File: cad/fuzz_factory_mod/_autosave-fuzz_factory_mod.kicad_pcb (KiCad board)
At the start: 4 copper layers, 138 x 114 mm, 390 parts, among them J101 Conn_interface_1, J102 Conn_interface_2, J1701 Barrel_Jack_Switch, J1702 Conn_Battery, J1703 CONN_AUDIO_IN, J1704 CONN_AUDIO_OUT, J201 Conn_MCU_SWD, J2801 CONN_AUDIO_OUT_REF, J2802 CONN_EXP_1, J2803 CONN_EXP_2, J301 USB_B_Micro, J401 USB_B_Micro, J901 CONN_MIDI_IN, J902 CONN_MIDI_THRU, J903 CONN_MIDI_OUT, J904 Conn_01x10_Female, J905 Conn_01x10_Female, K2101 Fujitsu-Takamisawa-A_AL, Q1301 MMDT3904, Q1302 MMDT3904, Q1602 DTA123Y, Q1603 DTA123Y, Q1604 DTA123Y, Q1605 DTA123Y, Q1701 DTC114Y, Q1702 DTA114E, Q2201 BCP51, Q601 DTA123Y, Q602 DTA123Y, Q603 DTA123Y, Q604 DTA123Y, Q801 MMDT3904, Q802 MMDT3904, SW1101 SW_PUSH, SW1201 SW_PUSH, SW1301 SW_PUSH, U1101 LM1458, U1102 MC33202, U1201 LM2903, U1202 MC33202, U1501 LM1458, U1502 MC33202, U1503 MC33202, U1601 4050, U1602 4049, U1603 4504, U1604 MC33202, U1701 LM1458, U1702 MC33202, U1803 LM1458, U1804 MC33202, U1901 LM2903, U201 STM32F303VCTx, U2201 TL072, U2202 LM2674M-ADJ, U2203 LM78L05_SO8, U301 USBLC6-2SC6, U302 FT230XS, U401 USBLC6-2SC6, U501 74LS132, U601 4050, U602 4504, U603 MC33202, U604 4049, U701 AD5262_ABC, U901 4N25, Y201 Resonator_Small

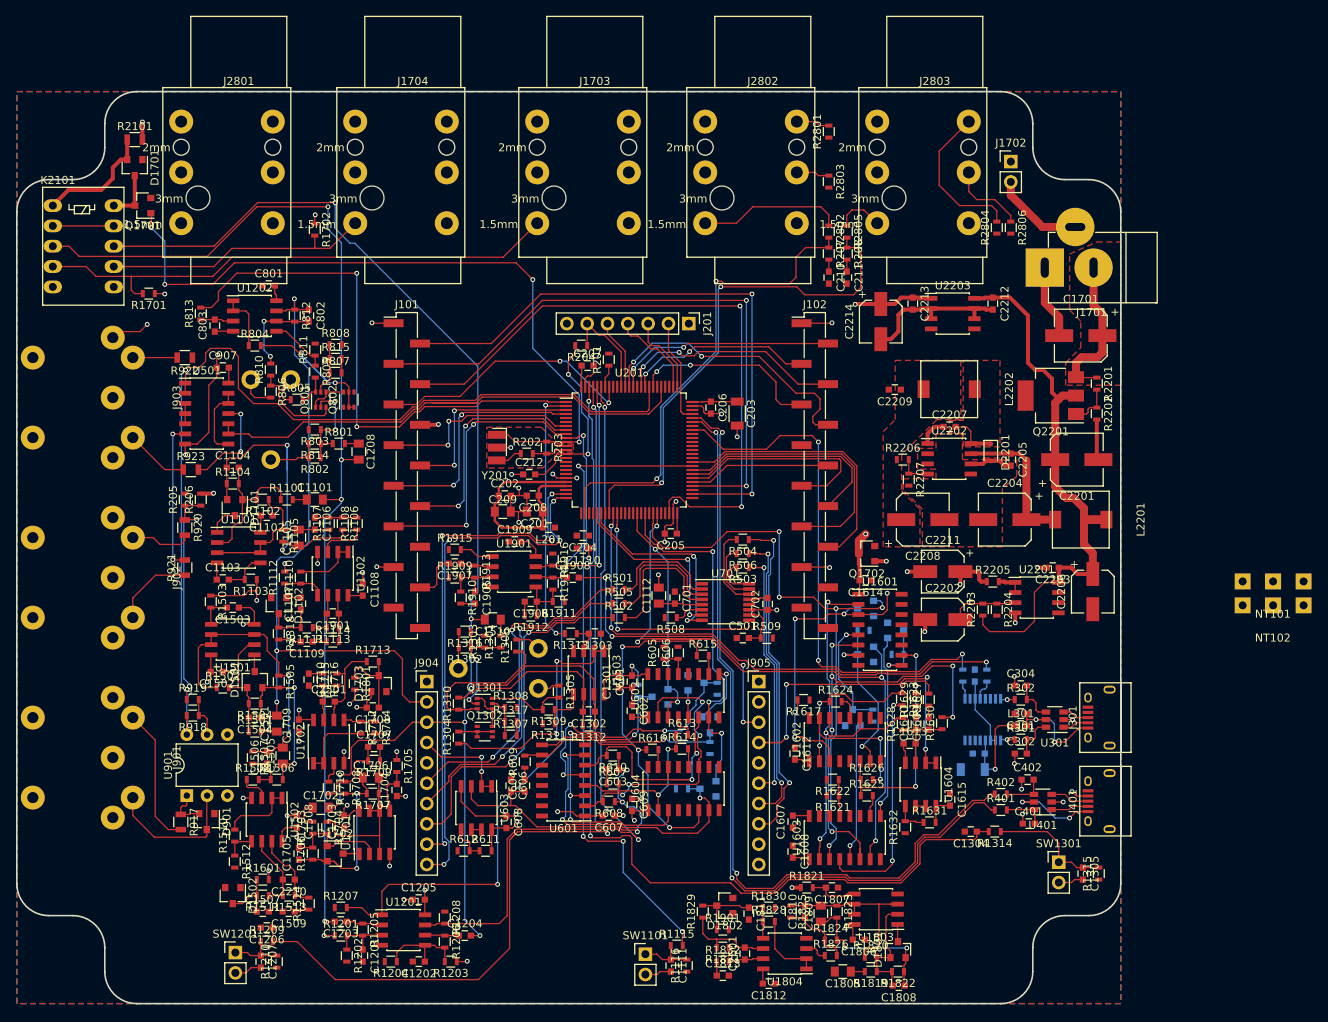
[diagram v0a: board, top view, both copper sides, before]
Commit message: Continued layout. Started power planes.
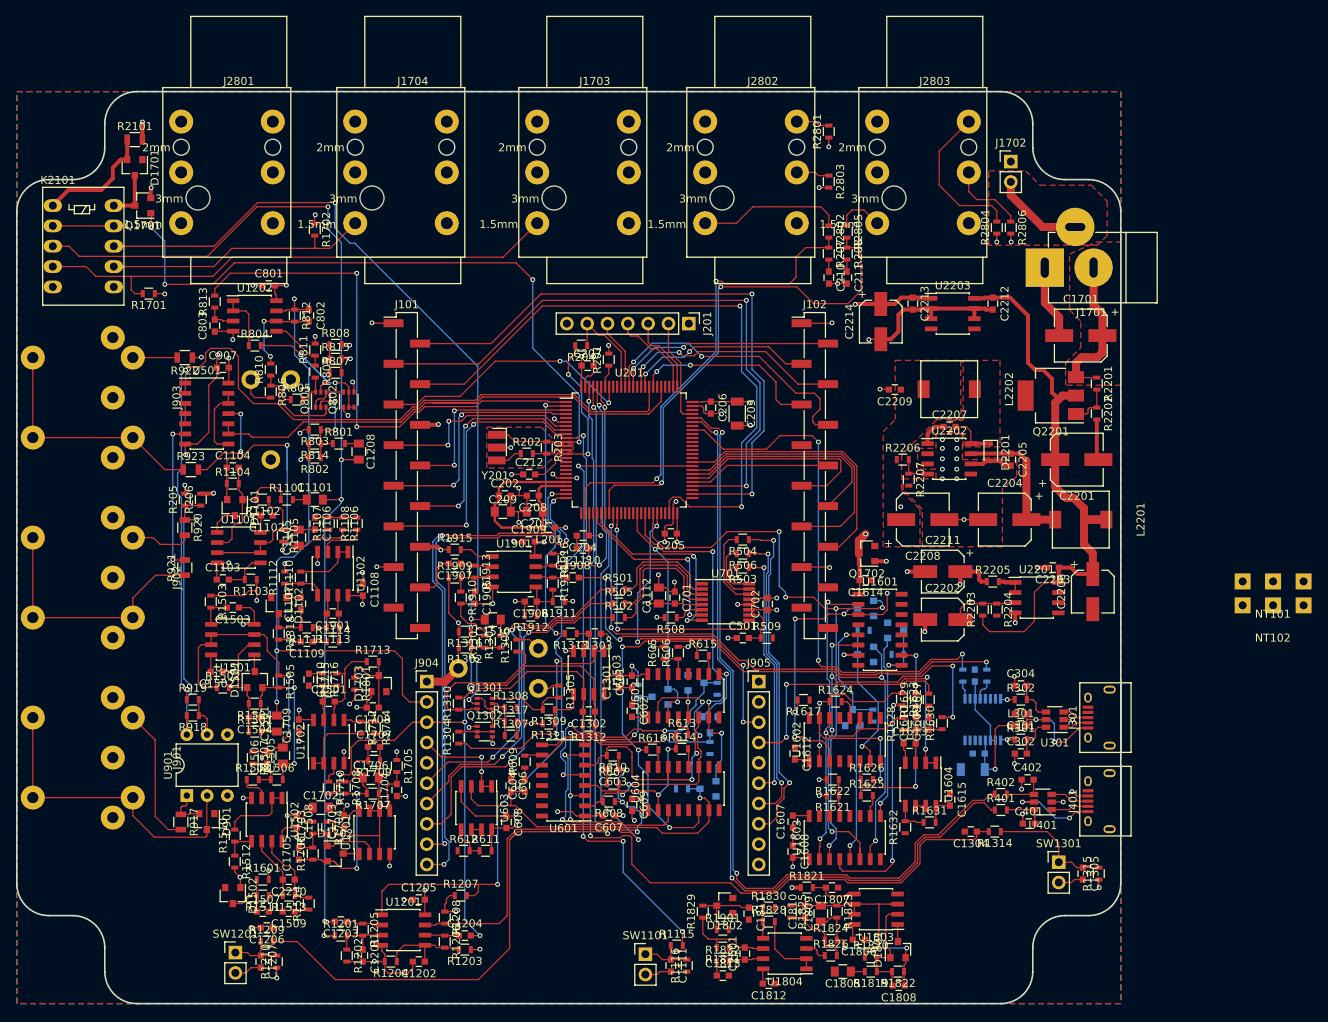
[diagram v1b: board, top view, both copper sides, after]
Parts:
- moved R1207 15.1 mm to (120.5, 133.0)
- moved R1203 2.30 mm to (121.0, 139.8)
- moved R813 2.30 mm to (89.8, 58.8)
- moved C1909 1.75 mm to (129.0, 88.8)
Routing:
- net +3V3: track 17.4 -> 612.9 mm, vias 0 -> 20
- net +9V: track 300.1 -> 559.0 mm, vias 15 -> 26
- net GNDA: track 78.0 -> 131.2 mm, vias 30 -> 53
- net /MCU/MIDI/+5V_IN: track 38.6 -> 76.8 mm, vias 1 -> 3
- net Net-(J902-Pad5): track 10.1 -> 32.6 mm
- net Net-(J903-Pad5): track 7.96 -> 30.5 mm
- net Net-(D901-Pad3): track 17.9 -> 40.4 mm
- net GNDD: track 103.2 -> 115.8 mm, vias 21 -> 39
- net VCOM: track 177.7 -> 189.3 mm
- net ADC_FF_pol2: track 65.4 -> 68.3 mm
- net ADC_FF_pol1: track 63.1 -> 65.7 mm
- net VCA_IN_PWM: track 68.7 -> 66.1 mm
- net INPUT_CAPTURE_1: track 93.8 -> 92.2 mm
- net DISP_ENABLE: track 80.5 -> 82.1 mm
- net SPI2_MOSI: track 77.3 -> 78.7 mm
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- added copper zone on In2.Cu, net +3V3
- added copper zone on In2.Cu, net +BATT
- added copper zone on F.Cu, net Net-(J1701-Pad3)
